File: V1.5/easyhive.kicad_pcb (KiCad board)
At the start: 2 copper layers, 35 x 75 mm, 106 parts, among them IC1 ATSAMD21G, IC2 BQ2407X, IC3 ADS1232, IC4 DS18B20U, IC5 XC6220B331, IC7 TPS22919, J1 U.FL, K1 693043020611, P1 PKMCS, Q1 32768 Hz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

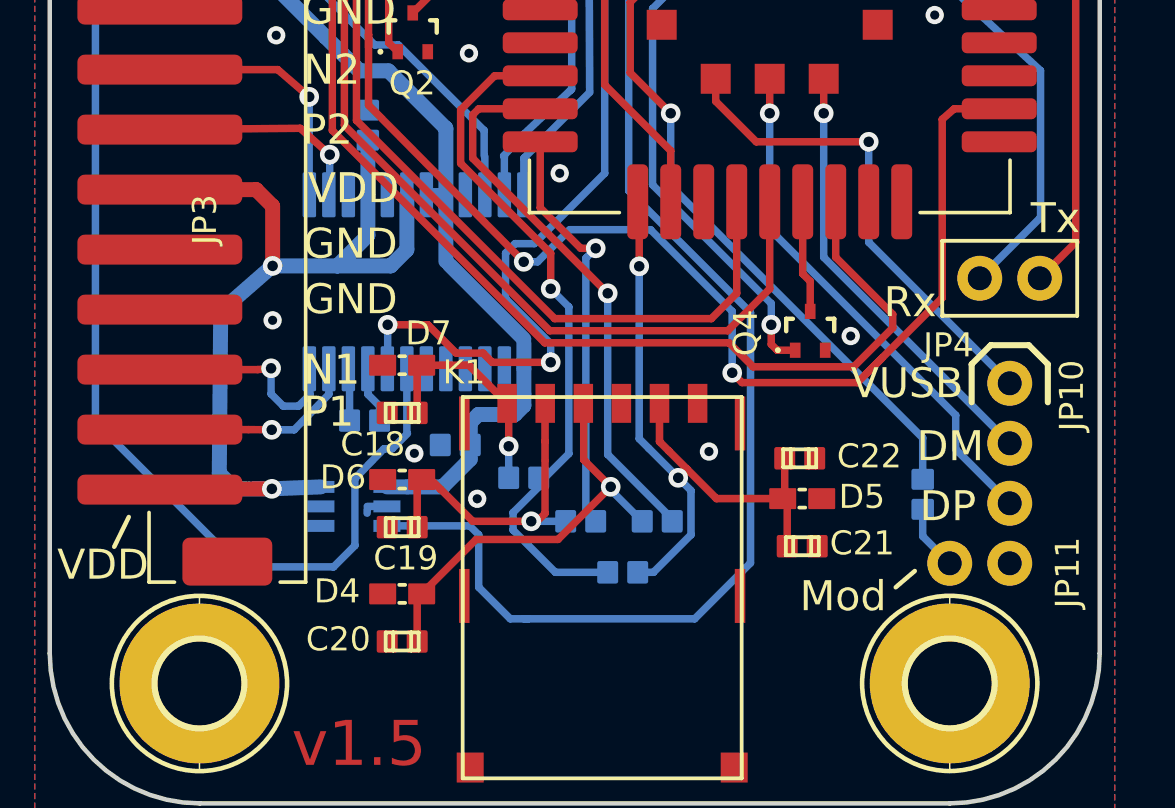
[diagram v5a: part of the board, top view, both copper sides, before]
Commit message: Add schmematic.pdf
-add easyhive-schematic.pdf
-rename C22 from 100nF to 100n
-remove text from JST PH Footprint
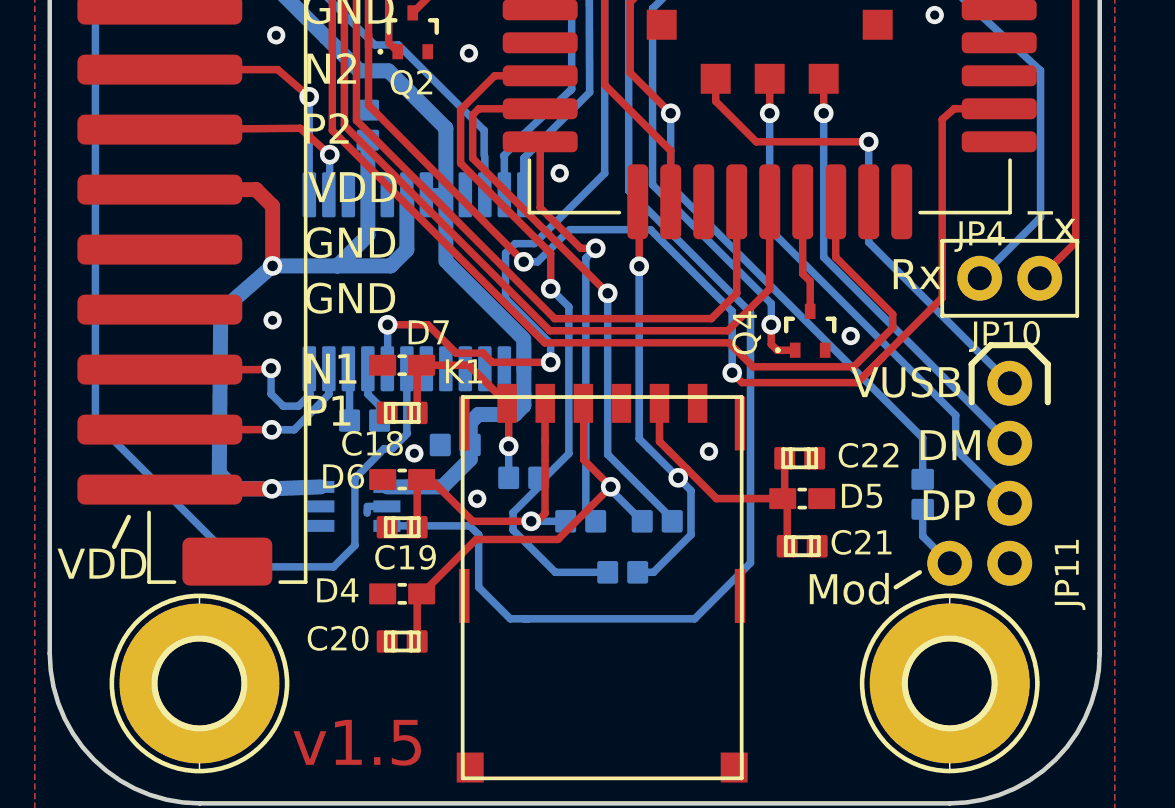
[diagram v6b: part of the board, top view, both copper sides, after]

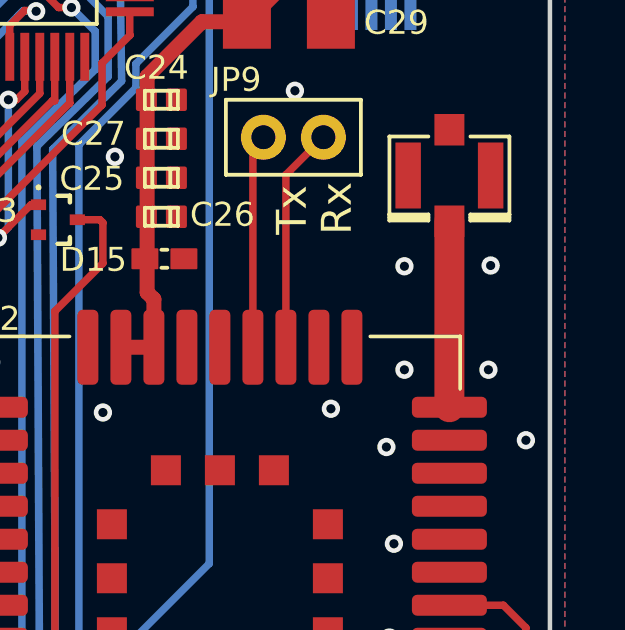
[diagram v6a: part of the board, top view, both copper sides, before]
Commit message: Track witdh antenna
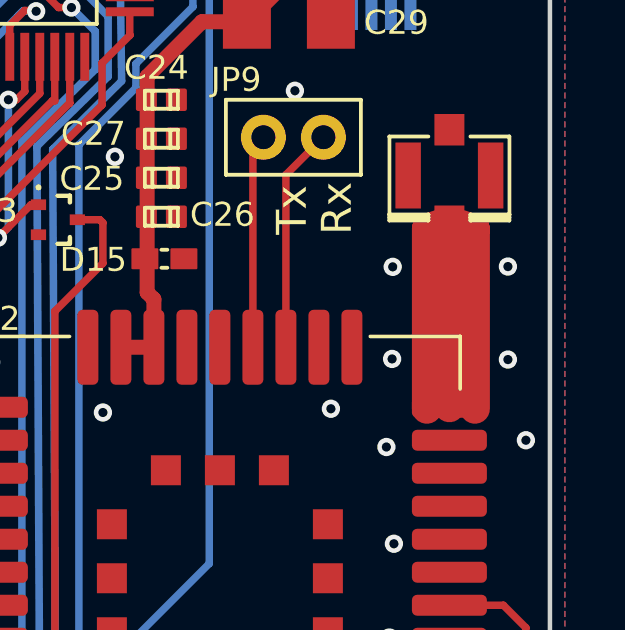
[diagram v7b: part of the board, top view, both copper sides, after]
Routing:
- net Net-(J1-PadP$3): track 6.20 -> 19.9 mm
